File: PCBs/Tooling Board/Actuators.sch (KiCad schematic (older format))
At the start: 10 parts

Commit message: Add DC Motor Control
-Added H-bridge drivers and logic inverters
-Should be able to control up to 6 DC motors / other loads
-We'll see if we can fit 3 chips on the board (we should be able to)
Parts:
- removed C?: 10000pF, symbol Device:C
- removed C?: 0.1uF, symbol Device:C
- removed C?: 100uF, symbol Device:CP
- removed C? (x2): 0.027uF, symbol Device:C
- removed D?: 40V, symbol Device:D_Zener
- removed M?: Motor_DC, symbol Motor:Motor_DC
- removed R?: 8.2K, symbol Device:R_US
- removed R?: 47K, symbol Device:R_US
- removed U?: TLE8209-2SA, symbol TLE8209-2SA:TLE8209-2SA
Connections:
- net labels removed: 12V_IN, 3.3V_IN, 5V_IN, Earth
- wire segments 56 -> 0
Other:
- note added: "Actuators"
- note added: "DCMotor1-2"
- note added: "DCMotor3-4"
- note added: "DCMotor5-6"
- note removed: "VDD GND"

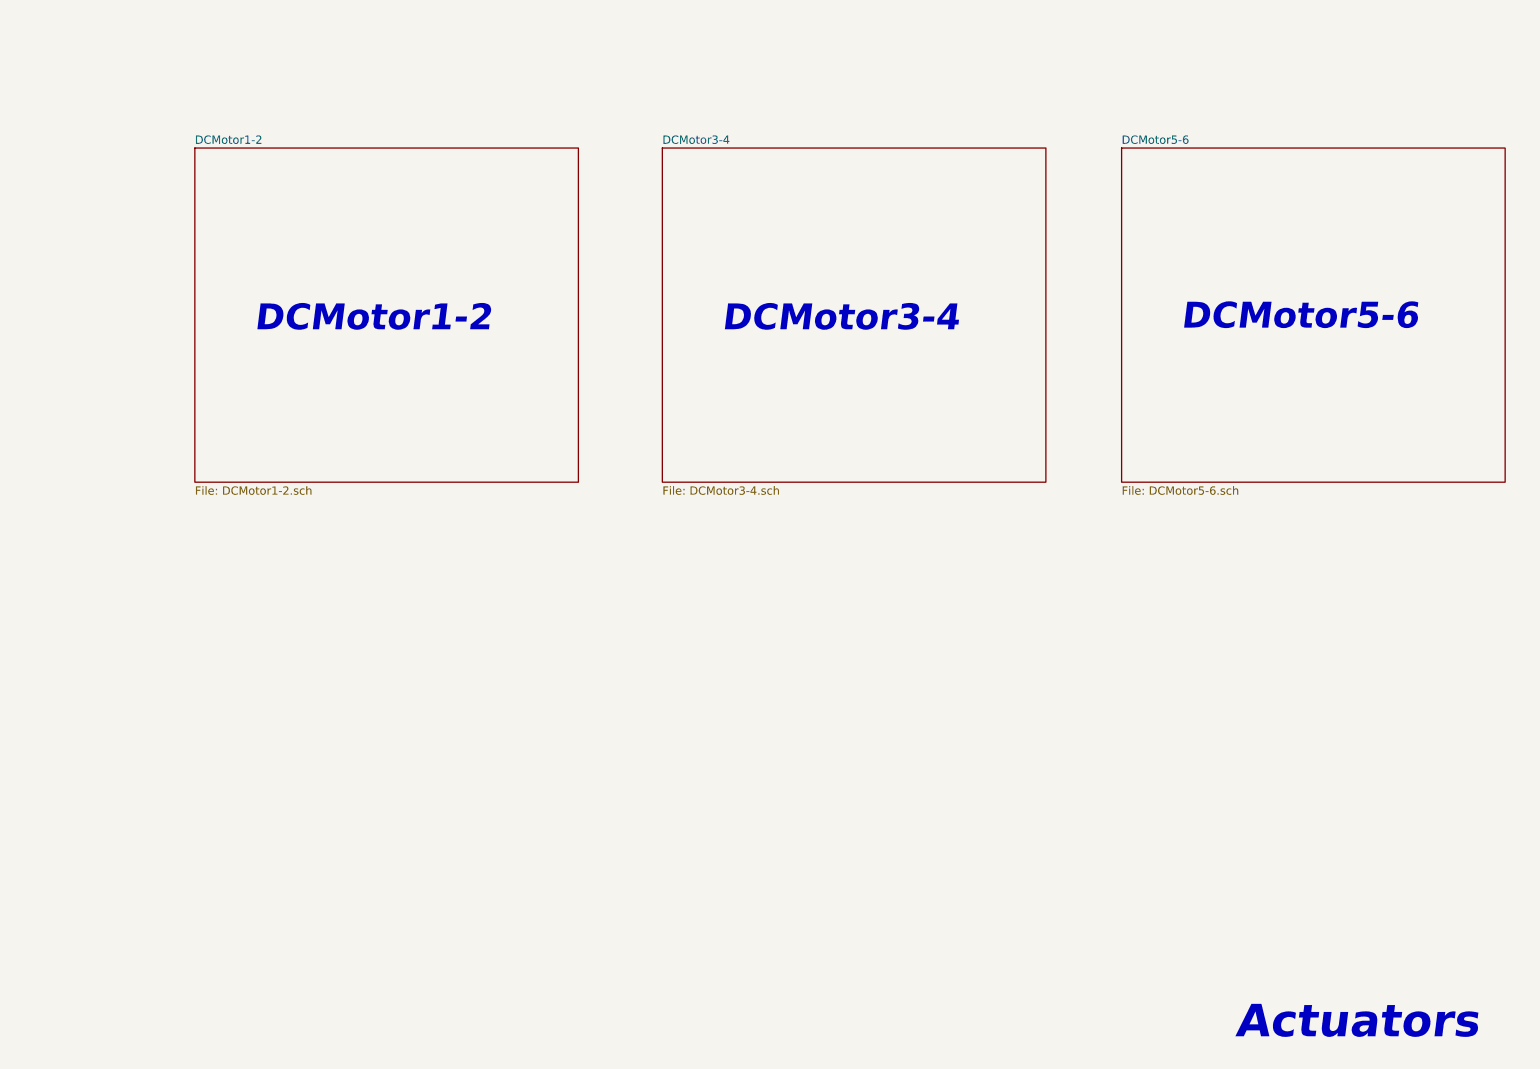
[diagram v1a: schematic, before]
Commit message: Finished Actuator Section
-Added Dual LED Control
-Spec'd fets for nmos in LED circuit
-Still need to map all control pins
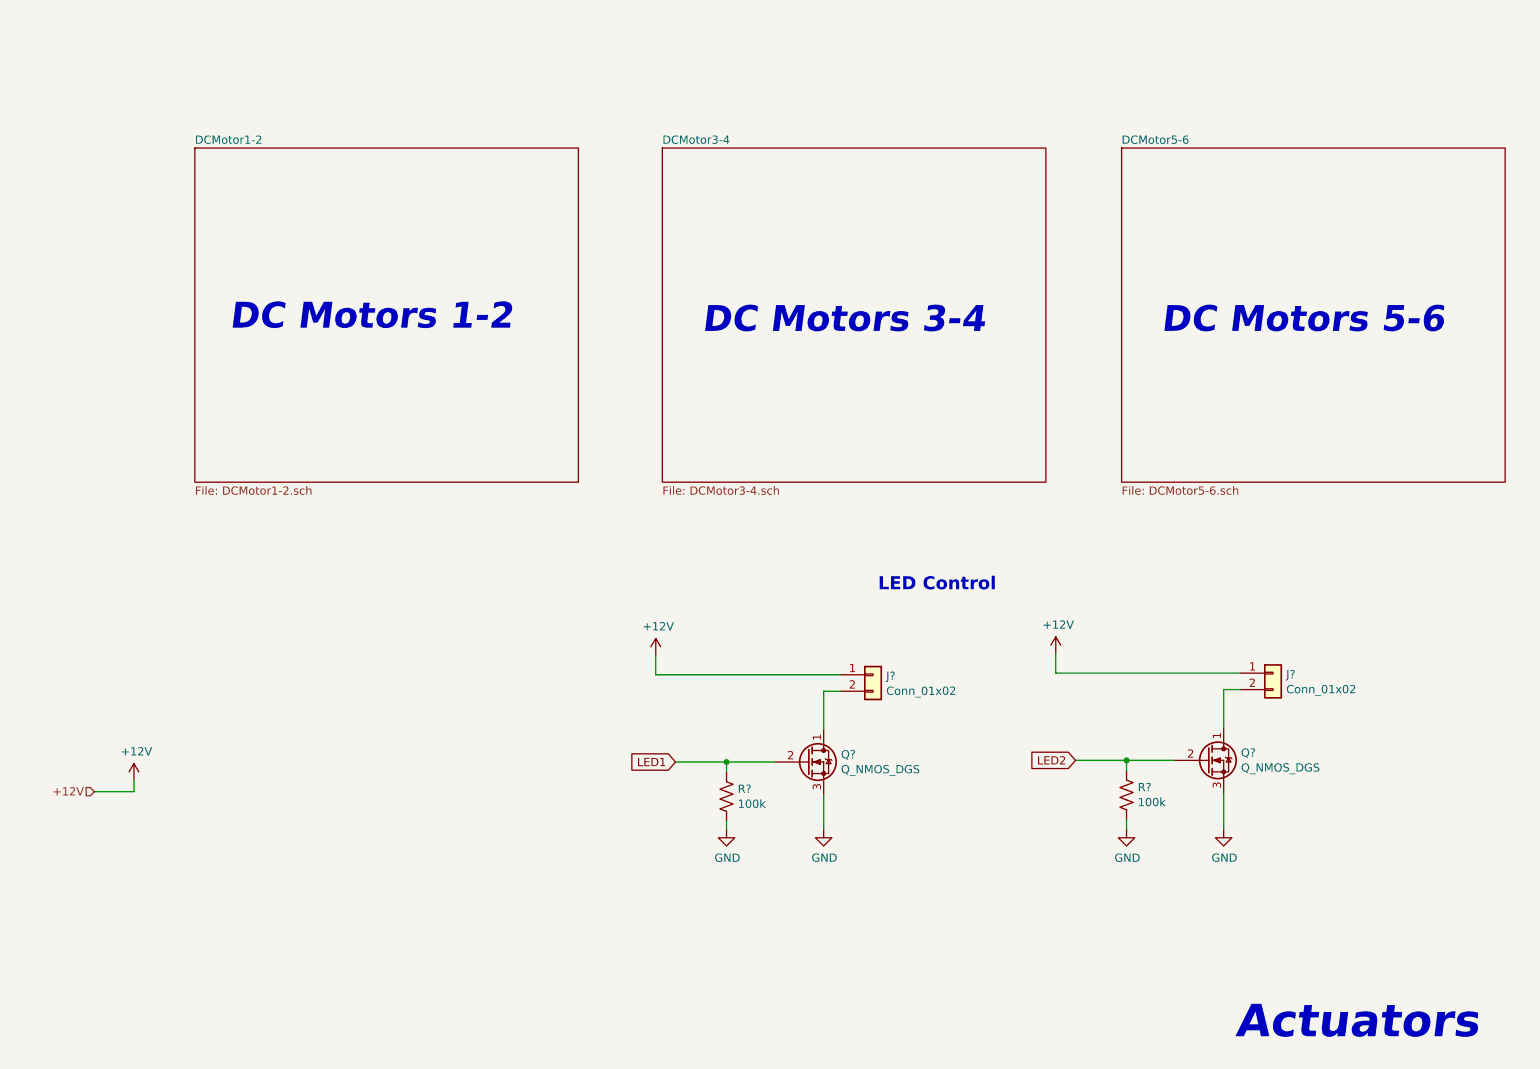
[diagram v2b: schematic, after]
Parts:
- added J? (x2): Conn_01x02, symbol Connector_Generic:Conn_01x02
- added Q? (x2): Q_NMOS_DGS, symbol Device:Q_NMOS_DGS
- added R? (x2): 100k, symbol Device:R_US
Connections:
- new net: J?.2 (Pin_2), Q?.1 (D) (x2)
- new net +12V: J?.1 (Pin_1), J?.1 (Pin_1)
- new net GND: Q?.3 (S), Q?.3 (S), R?.2, R?.2
- new net LED1: Q?.2 (G), R?.1
- new net LED2: Q?.2 (G), R?.1
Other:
- note added: "DC Motors 1-2"
- note added: "DC Motors 3-4"
- note added: "DC Motors 5-6"
- note added: "LED Control"
- note removed: "DCMotor1-2"
- note removed: "DCMotor3-4"
- note removed: "DCMotor5-6"
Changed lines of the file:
@@
 F1 "DCMotor1-2.sch" 50
 $EndSheet
-Text Notes 2380 2670 0    157  Italic 31
-DCMotor1-2
+Text Notes 2230 2660 0    157  Italic 31
+DC Motors 1-2
 $Sheet
 S 4860 1540 2330 2030
@@
 F1 "DCMotor3-4.sch" 50
 $EndSheet
-Text Notes 5220 2670 0    157  Italic 31
-DCMotor3-4
+Text Notes 5100 2680 0    157  Italic 31
+DC Motors 3-4
 $Sheet
 S 7650 1540 2330 2030
@@
 F1 "DCMotor5-6.sch" 50
 $EndSheet
-Text Notes 8010 2660 0    157  Italic 31
-DCMotor5-6
+Text Notes 7890 2680 0    157  Italic 31
+DC Motors 5-6
+Text HLabel 1410 5450 0    50   Input ~ 0
++12V
+Wire Wire Line
+	1410 5450 1650 5450
+Wire Wire Line
+	1650 5450 1650 5380
+$Comp
+L power:+12V #PWR?
+U 1 1 5C4DB93C
+P 1650 5380
+F 0 "#PWR?" H 1650 5230 50  0001 C CNN
+F 1 "+12V" H 1665 5553 50  0000 C CNN
+F 2 "" H 1650 5380 50  0001 C CNN
+F 3 "" H 1650 5380 50  0001 C CNN
+	1    1650 5380
+	1    0    0    -1
+$EndComp
+Text Notes 6170 4240 0    79   ~ 16
+LED Control
+$Comp
+L Connector_Generic:Conn_01x02 J?
+U 1 1 5C4DC4EB
+P 6140 4740
+F 0 "J?" H 6220 4732 50  0000 L CNN
+F 1 "Conn_01x02" H 6220 4641 50  0000 L CNN
+F 2 "" H 6140 4740 50  0001 C CNN
+F 3 "~" H 6140 4740 50  0001 C CNN
+	1    6140 4740
+	1    0    0    -1
+$EndComp
+Wire Wire Line
+	5940 4840 5840 4840
+$Comp
+L power:GND #PWR?
+U 1 1 5C4DC54D
+P 5840 5680
+F 0 "#PWR?" H 5840 5430 50  0001 C CNN
+F 1 "GND" H 5845 5507 50  0000 C CNN
+F 2 "" H 5840 5680 50  0001 C CNN
+F 3 "" H 5840 5680 50  0001 C CNN
+	1    5840 5680
+	1    0    0    -1
+$EndComp
+Wire Wire Line
+	4820 4740 4820 4620
+$Comp
+L power:+12V #PWR?
+U 1 1 5C4DC71D
+P 4820 4620
+F 0 "#PWR?" H 4820 4470 50  0001 C CNN
+F 1 "+12V" H 4835 4793 50  0000 C CNN
+F 2 "" H 4820 4620 50  0001 C CNN
+F 3 "" H 4820 4620 50  0001 C CNN
+	1    4820 4620
+	1    0    0    -1
+$EndComp
+$Comp
+L Device:Q_NMOS_DGS Q?
+U 1 1 5C4DC8F0
+P 5740 5270
+F 0 "Q?" H 5945 5316 50  0000 L CNN
+F 1 "Q_NMOS_DGS" H 5945 5225 50  0000 L CNN
+F 2 "" H 5940 5370 50  0001 C CNN
+F 3 "https://www.digikey.ca/product-detail/en/diodes-incorporated/DMN2020UFCL-7/DMN2020UFCL-7DICT-ND/4794805" H 5740 5270 50  0001 C CNN
+	1    5740 5270
+	1    0    0    -1
+$EndComp
+Wire Wire Line
+	5840 4840 5840 5070
+Wire Wire Line
+	5840 5470 5840 5680
+Wire Wire Line
+	5540 5270 5250 5270
+Wire Wire Line
+	4940 5270 5250 5270
+Text GLabel 4940 5270 0    50   Input ~ 0
+LED1
+$Comp
+L Connector_Generic:Conn_01x02 J?
+U 1 1 5C4DD714
+P 8570 4730
+F 0 "J?" H 8650 4722 50  0000 L CNN
+F 1 "Conn_01x02" H 8650 4631 50  0000 L CNN
+F 2 "" H 8570 4730 50  0001 C CNN
+F 3 "~" H 8570 4730 50  0001 C CNN
+	1    8570 4730
+	1    0    0    -1
+$EndComp
+Wire Wire Line
+	8370 4830 8270 4830
+$Comp
+L power:GND #PWR?
+U 1 1 5C4DD71B
+P 8270 5680
+F 0 "#PWR?" H 8270 5430 50  0001 C CNN
+F 1 "GND" H 8275 5507 50  0000 C CNN
+F 2 "" H 8270 5680 50  0001 C CNN
+F 3 "" H 8270 5680 50  0001 C CNN
+	1    8270 5680
+	1    0    0    -1
+$EndComp
+Wire Wire Line
+	7250 4730 7250 4610
+$Comp
+L power:+12V #PWR?
+U 1 1 5C4DD723
+P 7250 4610
+F 0 "#PWR?" H 7250 4460 50  0001 C CNN
+F 1 "+12V" H 7265 4783 50  0000 C CNN
+F 2 "" H 7250 4610 50  0001 C CNN
+F 3 "" H 7250 4610 50  0001 C CNN
+	1    7250 4610
+	1    0    0    -1
+$EndComp
+$Comp
+L Device:Q_NMOS_DGS Q?
+U 1 1 5C4DD729
+P 8170 5260
+F 0 "Q?" H 8375 5306 50  0000 L CNN
+F 1 "Q_NMOS_DGS" H 8375 5215 50  0000 L CNN
+F 2 "" H 8370 5360 50  0001 C CNN
+F 3 "https://www.digikey.ca/product-detail/en/diodes-incorporated/DMN2020UFCL-7/DMN2020UFCL-7DICT-ND/4794805" H 8170 5260 50  0001 C CNN
+	1    8170 5260
+	1    0    0    -1
+$EndComp
+Wire Wire Line
+	8270 4830 8270 5060
+Wire Wire Line
+	8270 5460 8270 5680
+Wire Wire Line
+	7970 5260 7680 5260
+Wire Wire Line
+	7370 5260 7680 5260
+Text GLabel 7370 5260 0    50   Input ~ 0
+LED2
+$Comp
+L Device:R_US R?
+U 1 1 5C4DDAFC
+P 5250 5480
+F 0 "R?" H 5318 5526 50  0000 L CNN
+F 1 "100k" H 5318 5435 50  0000 L CNN
+F 2 "" V 5290 5470 50  0001 C CNN
+F 3 "~" H 5250 5480 50  0001 C CNN
+	1    5250 5480
+	1    0    0    -1
+$EndComp
+$Comp
+L Device:R_US R?
+U 1 1 5C4DDB70
+P 7680 5470
+F 0 "R?" H 7748 5516 50  0000 L CNN
+F 1 "100k" H 7748 5425 50  0000 L CNN
+F 2 "" V 7720 5460 50  0001 C CNN
+F 3 "~" H 7680 5470 50  0001 C CNN
+	1    7680 5470
+	1    0    0    -1
+$EndComp
+Wire Wire Line
+	5250 5330 5250 5270
+Wire Wire Line
+	5250 5630 5250 5680
+$Comp
+L power:GND #PWR?
+U 1 1 5C4DDF92
+P 5250 5680
+F 0 "#PWR?" H 5250 5430 50  0001 C CNN
+F 1 "GND" H 5255 5507 50  0000 C CNN
+F 2 "" H 5250 5680 50  0001 C CNN
+F 3 "" H 5250 5680 50  0001 C CNN
+	1    5250 5680
+	1    0    0    -1
+$EndComp
+$Comp
+L power:GND #PWR?
+U 1 1 5C4DE205
+P 7680 5680
+F 0 "#PWR?" H 7680 5430 50  0001 C CNN
+F 1 "GND" H 7685 5507 50  0000 C CNN
+F 2 "" H 7680 5680 50  0001 C CNN
+F 3 "" H 7680 5680 50  0001 C CNN
+	1    7680 5680
+	1    0    0    -1
+$EndComp
+Wire Wire Line
+	7680 5680 7680 5620
+Wire Wire Line
+	7680 5320 7680 5260
+Wire Wire Line
+	7250 4730 8370 4730
+Wire Wire Line
+	4820 4740 5940 4740
+Connection ~ 5250 5270
+Connection ~ 7680 5260
 $EndSCHEMATC

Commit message: Pins are Mapped
-This was really difficult and it may not work.
-We're gonna try it and see what works.
-If it fails the next PCB will use arduino atmega chips since the open source libraries exist for them
-Might do a combination of SAMD and atmega lol
-God damn chinese new year
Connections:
- net LED2 is gone; now on net LED: Q?.2 (G), R?.1
- net LED1 renamed LED
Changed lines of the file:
@@
 EESchema Schematic File Version 4
-LIBS:Actuator Board-cache
+LIBS:Tooling Board-cache
 EELAYER 26 0
 EELAYER END
@@
 	4940 5270 5250 5270
 Text GLabel 4940 5270 0    50   Input ~ 0
-LED1
+LED
 $Comp
 L Connector_Generic:Conn_01x02 J?
@@
 Wire Wire Line
 	7370 5260 7680 5260
-Text GLabel 7370 5260 0    50   Input ~ 0
-LED2
 $Comp
 L Device:R_US R?
@@
 Connection ~ 5250 5270
 Connection ~ 7680 5260
+Text GLabel 7370 5260 0    50   Input ~ 0
+LED
 $EndSCHEMATC

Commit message: Added Footprints
-Whoooo boy here we go
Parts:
- J301, J302: renamed from J?; footprint (none) -> Junction Box:70553-02
- Q301, Q302: renamed from Q?; footprint (none) -> EER:TRANS_DMN2020UFCL-7
- R301, R302: renamed from R?; footprint (none) -> Resistors_SMD:R_0805_HandSoldering
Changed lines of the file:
@@
 	1650 5450 1650 5380
 $Comp
-L power:+12V #PWR?
+L power:+12V #PWR0127
 U 1 1 5C4DB93C
 P 1650 5380
-F 0 "#PWR?" H 1650 5230 50  0001 C CNN
+F 0 "#PWR0127" H 1650 5230 50  0001 C CNN
 F 1 "+12V" H 1665 5553 50  0000 C CNN
 F 2 "" H 1650 5380 50  0001 C CNN
@@
 LED Control
 $Comp
-L Connector_Generic:Conn_01x02 J?
+L Connector_Generic:Conn_01x02 J301
 U 1 1 5C4DC4EB
 P 6140 4740
-F 0 "J?" H 6220 4732 50  0000 L CNN
+F 0 "J301" H 6220 4732 50  0000 L CNN
 F 1 "Conn_01x02" H 6220 4641 50  0000 L CNN
-F 2 "" H 6140 4740 50  0001 C CNN
+F 2 "Junction Box:70553-02" H 6140 4740 50  0001 C CNN
 F 3 "~" H 6140 4740 50  0001 C CNN
 	1    6140 4740
@@
 	5940 4840 5840 4840
 $Comp
-L power:GND #PWR?
+L power:GND #PWR0128
 U 1 1 5C4DC54D
 P 5840 5680
-F 0 "#PWR?" H 5840 5430 50  0001 C CNN
+F 0 "#PWR0128" H 5840 5430 50  0001 C CNN
 F 1 "GND" H 5845 5507 50  0000 C CNN
 F 2 "" H 5840 5680 50  0001 C CNN
@@
 	4820 4740 4820 4620
 $Comp
-L power:+12V #PWR?
+L power:+12V #PWR0129
 U 1 1 5C4DC71D
 P 4820 4620
-F 0 "#PWR?" H 4820 4470 50  0001 C CNN
+F 0 "#PWR0129" H 4820 4470 50  0001 C CNN
 F 1 "+12V" H 4835 4793 50  0000 C CNN
 F 2 "" H 4820 4620 50  0001 C CNN
@@
 $EndComp
 $Comp
-L Device:Q_NMOS_DGS Q?
+L Device:Q_NMOS_DGS Q301
 U 1 1 5C4DC8F0
 P 5740 5270
-F 0 "Q?" H 5945 5316 50  0000 L CNN
+F 0 "Q301" H 5945 5316 50  0000 L CNN
 F 1 "Q_NMOS_DGS" H 5945 5225 50  0000 L CNN
-F 2 "" H 5940 5370 50  0001 C CNN
+F 2 "EER:TRANS_DMN2020UFCL-7" H 5940 5370 50  0001 C CNN
 F 3 "https://www.digikey.ca/product-detail/en/diodes-incorporated/DMN2020UFCL-7/DMN2020UFCL-7DICT-ND/4794805" H 5740 5270 50  0001 C CNN
 	1    5740 5270
@@
 LED
 $Comp
-L Connector_Generic:Conn_01x02 J?
+L Connector_Generic:Conn_01x02 J302
 U 1 1 5C4DD714
 P 8570 4730
-F 0 "J?" H 8650 4722 50  0000 L CNN
+F 0 "J302" H 8650 4722 50  0000 L CNN
 F 1 "Conn_01x02" H 8650 4631 50  0000 L CNN
-F 2 "" H 8570 4730 50  0001 C CNN
+F 2 "Junction Box:70553-02" H 8570 4730 50  0001 C CNN
 F 3 "~" H 8570 4730 50  0001 C CNN
 	1    8570 4730
@@
 	8370 4830 8270 4830
 $Comp
-L power:GND #PWR?
+L power:GND #PWR0130
 U 1 1 5C4DD71B
 P 8270 5680
-F 0 "#PWR?" H 8270 5430 50  0001 C CNN
+F 0 "#PWR0130" H 8270 5430 50  0001 C CNN
 F 1 "GND" H 8275 5507 50  0000 C CNN
 F 2 "" H 8270 5680 50  0001 C CNN
@@
 	7250 4730 7250 4610
 $Comp
-L power:+12V #PWR?
+L power:+12V #PWR0131
 U 1 1 5C4DD723
 P 7250 4610
-F 0 "#PWR?" H 7250 4460 50  0001 C CNN
+F 0 "#PWR0131" H 7250 4460 50  0001 C CNN
 F 1 "+12V" H 7265 4783 50  0000 C CNN
 F 2 "" H 7250 4610 50  0001 C CNN
@@
 $EndComp
 $Comp
-L Device:Q_NMOS_DGS Q?
+L Device:Q_NMOS_DGS Q302
 U 1 1 5C4DD729
 P 8170 5260
-F 0 "Q?" H 8375 5306 50  0000 L CNN
+F 0 "Q302" H 8375 5306 50  0000 L CNN
 F 1 "Q_NMOS_DGS" H 8375 5215 50  0000 L CNN
-F 2 "" H 8370 5360 50  0001 C CNN
+F 2 "EER:TRANS_DMN2020UFCL-7" H 8370 5360 50  0001 C CNN
 F 3 "https://www.digikey.ca/product-detail/en/diodes-incorporated/DMN2020UFCL-7/DMN2020UFCL-7DICT-ND/4794805" H 8170 5260 50  0001 C CNN
 	1    8170 5260
@@
 	7370 5260 7680 5260
 $Comp
-L Device:R_US R?
+L Device:R_US R301
 U 1 1 5C4DDAFC
 P 5250 5480
-F 0 "R?" H 5318 5526 50  0000 L CNN
+F 0 "R301" H 5318 5526 50  0000 L CNN
 F 1 "100k" H 5318 5435 50  0000 L CNN
-F 2 "" V 5290 5470 50  0001 C CNN
+F 2 "Resistors_SMD:R_0805_HandSoldering" V 5290 5470 50  0001 C CNN
 F 3 "~" H 5250 5480 50  0001 C CNN
 	1    5250 5480
@@
 $EndComp
 $Comp
-L Device:R_US R?
+L Device:R_US R302
 U 1 1 5C4DDB70
 P 7680 5470
-F 0 "R?" H 7748 5516 50  0000 L CNN
+F 0 "R302" H 7748 5516 50  0000 L CNN
 F 1 "100k" H 7748 5425 50  0000 L CNN
-F 2 "" V 7720 5460 50  0001 C CNN
+F 2 "Resistors_SMD:R_0805_HandSoldering" V 7720 5460 50  0001 C CNN
 F 3 "~" H 7680 5470 50  0001 C CNN
 	1    7680 5470
@@
 	5250 5630 5250 5680
 $Comp
-L power:GND #PWR?
+L power:GND #PWR0132
 U 1 1 5C4DDF92
 P 5250 5680
-F 0 "#PWR?" H 5250 5430 50  0001 C CNN
+F 0 "#PWR0132" H 5250 5430 50  0001 C CNN
 F 1 "GND" H 5255 5507 50  0000 C CNN
 F 2 "" H 5250 5680 50  0001 C CNN
@@
 $EndComp
 $Comp
-L power:GND #PWR?
+L power:GND #PWR0133
 U 1 1 5C4DE205
 P 7680 5680
-F 0 "#PWR?" H 7680 5430 50  0001 C CNN
+F 0 "#PWR0133" H 7680 5430 50  0001 C CNN
 F 1 "GND" H 7685 5507 50  0000 C CNN
 F 2 "" H 7680 5680 50  0001 C CNN

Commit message: Removed 3rd DC Motor Driver
-Can only do 4 DC motors now, not enough board space
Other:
- note removed: "DC Motors 5-6"
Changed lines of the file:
@@
 $Descr A4 11693 8268
 encoding utf-8
-Sheet 3 8
+Sheet 3 7
 Title ""
 Date ""
@@
 Text Notes 5100 2680 0    157  Italic 31
 DC Motors 3-4
-$Sheet
-S 7650 1540 2330 2030
-U 5C4D49A1
-F0 "DCMotor5-6" 50
-F1 "DCMotor5-6.sch" 50
-$EndSheet
-Text Notes 7890 2680 0    157  Italic 31
-DC Motors 5-6
 Text HLabel 1410 5450 0    50   Input ~ 0
 +12V

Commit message: Almost Finished
-Still going, help
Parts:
- removed R301, R302: 100k, Resistors_SMD:R_0805_HandSoldering, symbol Device:R_US
- J301, J302: footprint Junction Box:70553-02 -> EER:1x2_molex_llc_new
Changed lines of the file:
@@
 F 0 "J301" H 6220 4732 50  0000 L CNN
 F 1 "Conn_01x02" H 6220 4641 50  0000 L CNN
-F 2 "Junction Box:70553-02" H 6140 4740 50  0001 C CNN
+F 2 "EER:1x2_molex_llc_new" H 6140 4740 50  0001 C CNN
 F 3 "~" H 6140 4740 50  0001 C CNN
 	1    6140 4740
@@
 Wire Wire Line
 	5840 5470 5840 5680
-Wire Wire Line
-	5540 5270 5250 5270
-Wire Wire Line
-	4940 5270 5250 5270
 Text GLabel 4940 5270 0    50   Input ~ 0
 LED
@@
 F 0 "J302" H 8650 4722 50  0000 L CNN
 F 1 "Conn_01x02" H 8650 4631 50  0000 L CNN
-F 2 "Junction Box:70553-02" H 8570 4730 50  0001 C CNN
+F 2 "EER:1x2_molex_llc_new" H 8570 4730 50  0001 C CNN
 F 3 "~" H 8570 4730 50  0001 C CNN
 	1    8570 4730
@@
 	8270 5460 8270 5680
 Wire Wire Line
-	7970 5260 7680 5260
-Wire Wire Line
-	7370 5260 7680 5260
-$Comp
-L Device:R_US R301
-U 1 1 5C4DDAFC
-P 5250 5480
-F 0 "R301" H 5318 5526 50  0000 L CNN
-F 1 "100k" H 5318 5435 50  0000 L CNN
-F 2 "Resistors_SMD:R_0805_HandSoldering" V 5290 5470 50  0001 C CNN
-F 3 "~" H 5250 5480 50  0001 C CNN
-	1    5250 5480
-	1    0    0    -1
-$EndComp
-$Comp
-L Device:R_US R302
-U 1 1 5C4DDB70
-P 7680 5470
-F 0 "R302" H 7748 5516 50  0000 L CNN
-F 1 "100k" H 7748 5425 50  0000 L CNN
-F 2 "Resistors_SMD:R_0805_HandSoldering" V 7720 5460 50  0001 C CNN
-F 3 "~" H 7680 5470 50  0001 C CNN
-	1    7680 5470
-	1    0    0    -1
-$EndComp
-Wire Wire Line
-	5250 5330 5250 5270
-Wire Wire Line
-	5250 5630 5250 5680
-$Comp
-L power:GND #PWR0132
-U 1 1 5C4DDF92
-P 5250 5680
-F 0 "#PWR0132" H 5250 5430 50  0001 C CNN
-F 1 "GND" H 5255 5507 50  0000 C CNN
-F 2 "" H 5250 5680 50  0001 C CNN
-F 3 "" H 5250 5680 50  0001 C CNN
-	1    5250 5680
-	1    0    0    -1
-$EndComp
-$Comp
-L power:GND #PWR0133
-U 1 1 5C4DE205
-P 7680 5680
-F 0 "#PWR0133" H 7680 5430 50  0001 C CNN
-F 1 "GND" H 7685 5507 50  0000 C CNN
-F 2 "" H 7680 5680 50  0001 C CNN
-F 3 "" H 7680 5680 50  0001 C CNN
-	1    7680 5680
-	1    0    0    -1
-$EndComp
-Wire Wire Line
-	7680 5680 7680 5620
-Wire Wire Line
-	7680 5320 7680 5260
-Wire Wire Line
 	7250 4730 8370 4730
 Wire Wire Line
 	4820 4740 5940 4740
-Connection ~ 5250 5270
-Connection ~ 7680 5260
 Text GLabel 7370 5260 0    50   Input ~ 0
 LED
+Wire Wire Line
+	7370 5260 7970 5260
+Wire Wire Line
+	4940 5270 5540 5270
 $EndSCHEMATC

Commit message: tooling board bom
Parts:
- J301, J302: Digikey (none) -> WM4800-ND
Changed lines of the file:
@@
 F 2 "EER:1x2_molex_llc_new" H 6140 4740 50  0001 C CNN
 F 3 "~" H 6140 4740 50  0001 C CNN
+F 4 "WM4800-ND" H 6140 4740 50  0001 C CNN "Digikey"
 	1    6140 4740
 	1    0    0    -1
@@
 F 2 "EER:1x2_molex_llc_new" H 8570 4730 50  0001 C CNN
 F 3 "~" H 8570 4730 50  0001 C CNN
+F 4 "WM4800-ND" H 8570 4730 50  0001 C CNN "Digikey"
 	1    8570 4730
 	1    0    0    -1
